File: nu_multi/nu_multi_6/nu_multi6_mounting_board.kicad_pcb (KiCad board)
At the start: 2 copper layers, 70 x 18.2 mm, 14 parts, among them J1 CONN_01X02, J10 CONN_01X03, J11 CONN_01X02, J12 CONN_01X03, J13 CONN_01X14, J2 CONN_01X03, J3 CONN_01X02, J4 CONN_01X03, J5 CONN_01X02, J6 CONN_01X03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

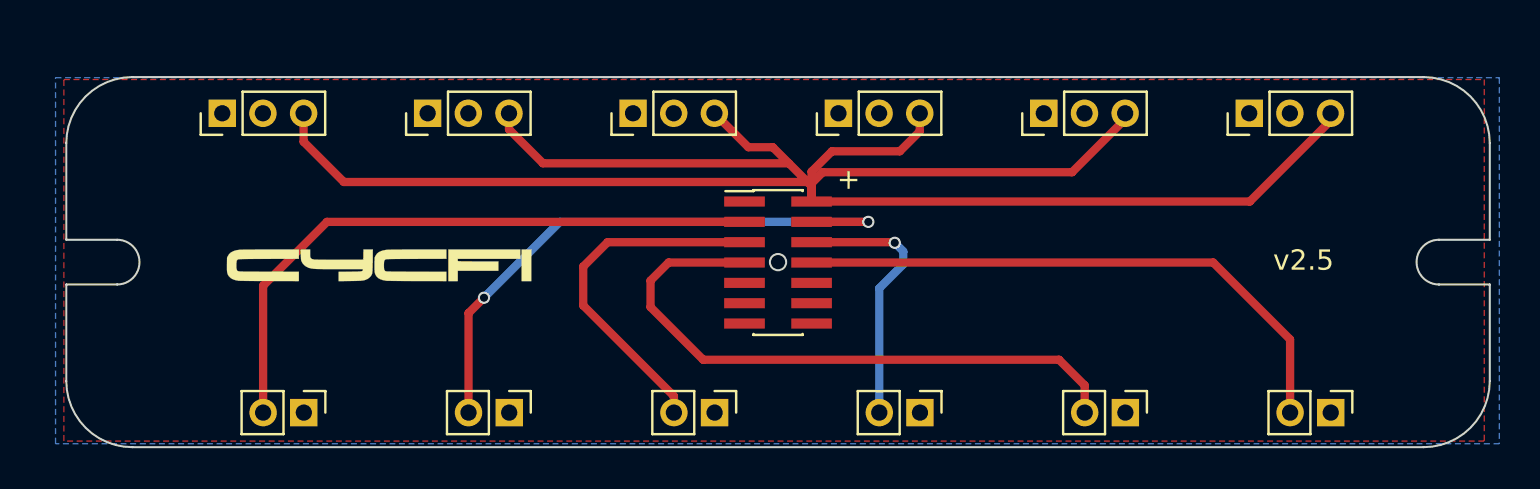
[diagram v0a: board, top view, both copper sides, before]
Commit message: perfect alignment; fixed sloppy positioning
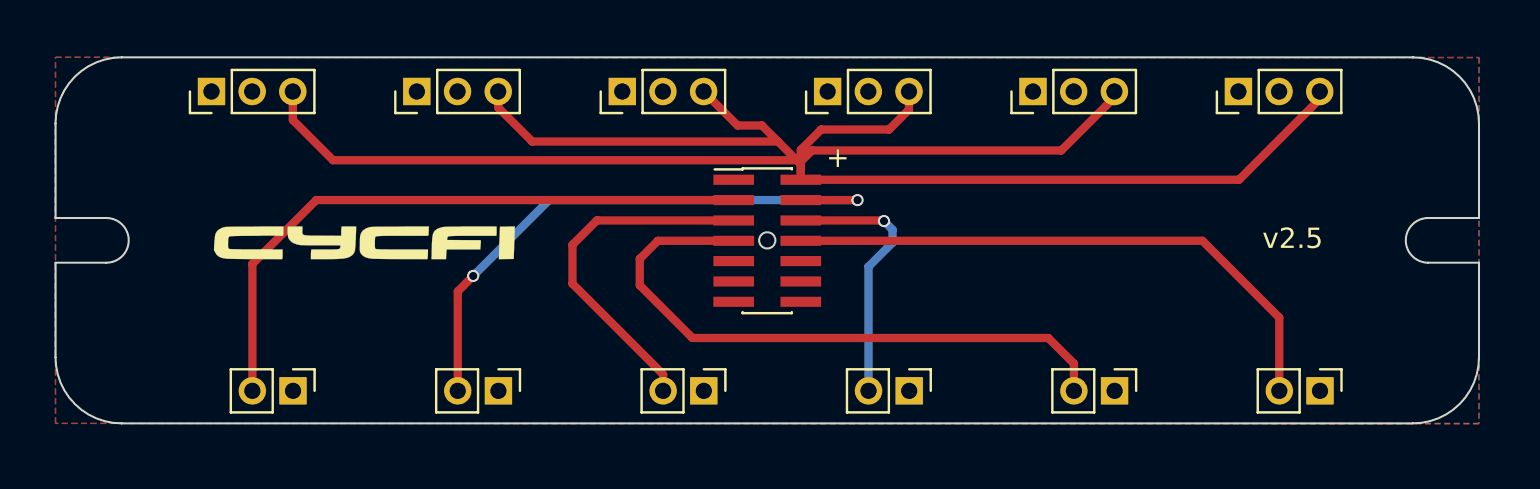
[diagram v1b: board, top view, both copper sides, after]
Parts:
- removed the G*** at (120.9, 94.2)
- added G***: LOGO, cycfi_library:cycfi-logo-15mm, F.Cu at (120.1, 93.2)
- moved J13 1.19 mm to (140.0, 93.0)
- moved J1 1.19 mm to (157.1, 100.4)
- moved J10 1.19 mm to (112.7, 85.7)
- moved J11 1.19 mm to (167.2, 100.4)
- moved J12 1.19 mm to (163.2, 85.7)
- moved J2 1.19 mm to (153.1, 85.7)
- moved J3 1.19 mm to (147.0, 100.4)
- moved J4 1.19 mm to (143.0, 85.7)
- moved J5 1.19 mm to (136.9, 100.4)
- moved J6 1.19 mm to (132.9, 85.7)
- moved J7 1.19 mm to (126.8, 100.4)
- moved J8 1.19 mm to (122.8, 85.7)
- moved J9 1.19 mm to (116.7, 100.4)
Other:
- board size 70 x 18.2 mm -> 70 x 18 mm

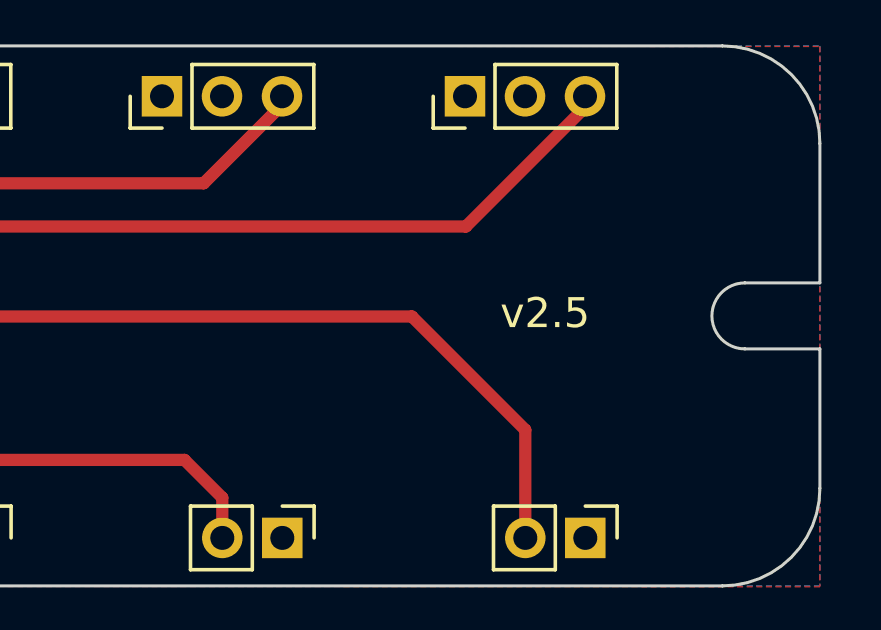
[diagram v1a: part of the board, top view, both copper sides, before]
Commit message: Updates; added nu multi-8 mounting board
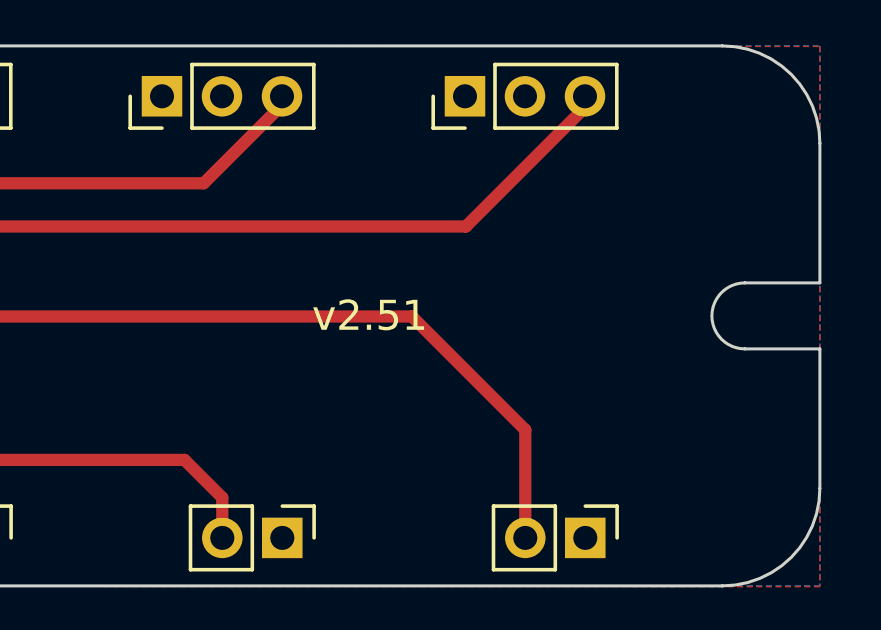
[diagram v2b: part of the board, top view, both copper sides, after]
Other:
- board text added: "v2.51"
- board text removed: "v2.5"

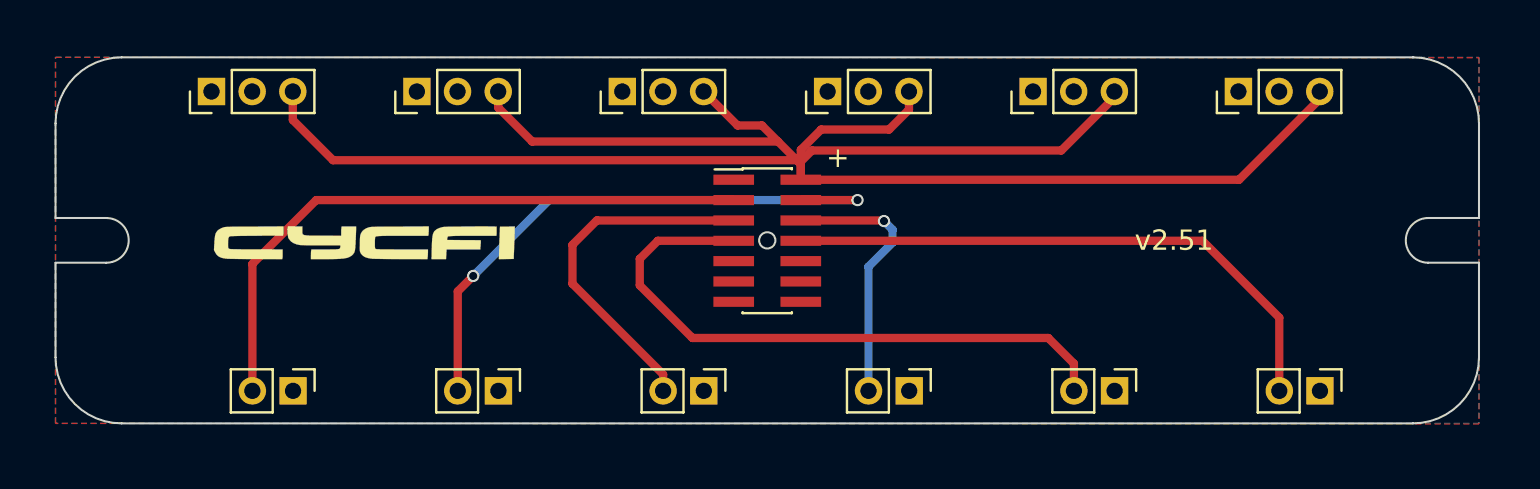
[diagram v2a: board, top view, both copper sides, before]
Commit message: Upgrade to KiCad 6
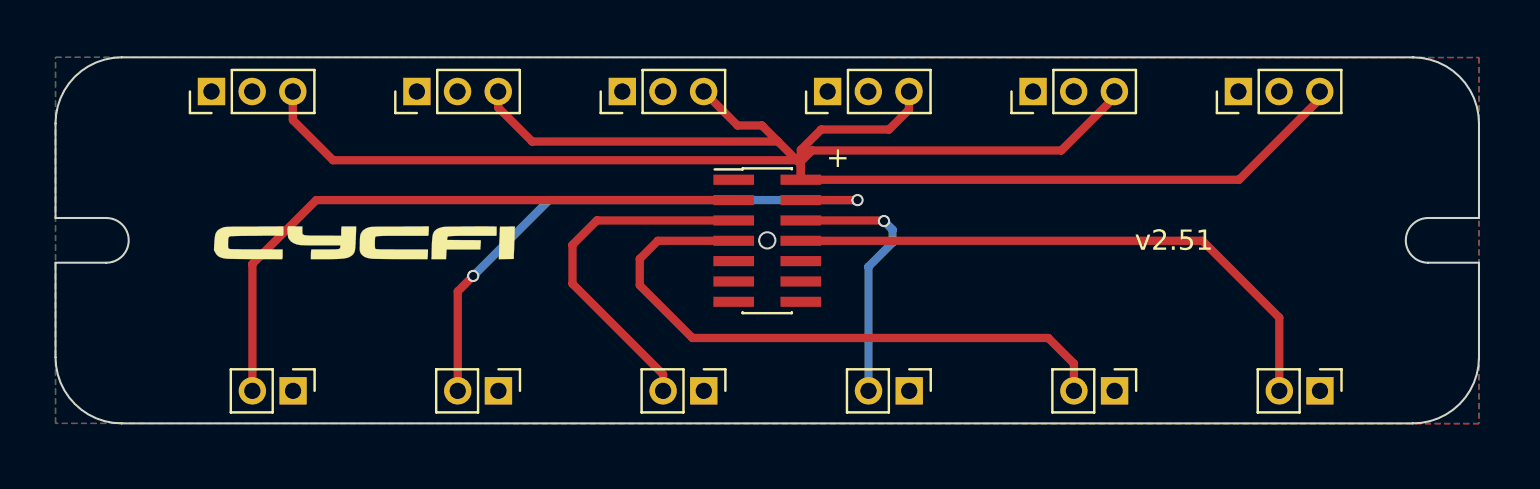
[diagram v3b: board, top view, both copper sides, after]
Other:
- net class Default removed

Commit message: Upgraded schematics and PCB layout using Nu Capsule footprint
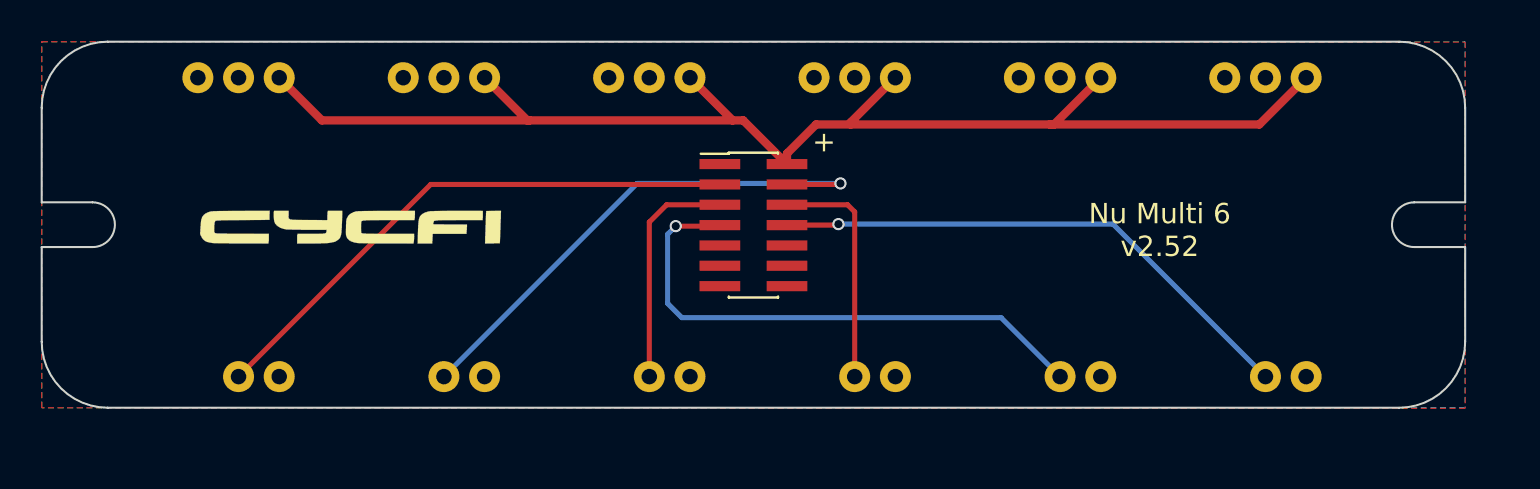
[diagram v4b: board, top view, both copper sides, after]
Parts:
- removed J1, J11, J3, J5, J7, J9: CONN_01X02, Pin_Headers:Pin_Header_Straight_1x02_Pitch2.00mm
- removed J10, J12, J2, J4, J6, J8: CONN_01X03, Pin_Headers:Pin_Header_Straight_1x03_Pitch2.00mm
- added U1: nu_capsule, cycfi_library:nu_capsule, F.Cu at (112.0, 85.0)
- added U2: nu_capsule, cycfi_library:nu_capsule, F.Cu at (122.1, 85.0)
- added U3: nu_capsule, cycfi_library:nu_capsule, F.Cu at (132.2, 85.0)
- added U4: nu_capsule, cycfi_library:nu_capsule, F.Cu at (142.3, 85.0)
- added U5: nu_capsule, cycfi_library:nu_capsule, F.Cu at (152.4, 85.0)
- added U6: nu_capsule, cycfi_library:nu_capsule, F.Cu at (162.5, 85.0)
- moved G*** 1.03 mm to (119.4, 92.4)
- moved J13 1.03 mm to (139.3, 92.2)
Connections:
- J13 pad 10: Net-(J13-Pad10) -> unconnected-(J13-Pad10)
- J13 pad 3: Net-(J13-Pad3) -> CH1
- J13 pad 4: Net-(J13-Pad4) -> CH2
- J13 pad 5: Net-(J13-Pad5) -> CH3
- J13 pad 6: Net-(J13-Pad6) -> CH4
- J13 pad 7: Net-(J1-Pad2) -> CH5
- J13 pad 8: Net-(J11-Pad2) -> CH6
- J13 pad 9: Net-(J13-Pad9) -> unconnected-(J13-Pad9)
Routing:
- net V+: track 102.5 -> 67.0 mm
- net Net-(J13-Pad3): track 31.2 -> 0.00 mm
- net Net-(J1-Pad2): track 30.6 -> 0.00 mm
- net Net-(J13-Pad4): track 29.2 -> 0.00 mm, vias 2 -> 0
- net Net-(J11-Pad2): track 28.7 -> 0.00 mm
- net CH1: track 0.00 -> 27.6 mm
- net CH5: track 0.00 -> 26.9 mm, vias 0 -> 1
- net CH6: track 0.00 -> 26.7 mm, vias 0 -> 1
- net CH2: track 0.00 -> 26.1 mm, vias 0 -> 1
- net Net-(J13-Pad5): track 17.5 -> 0.00 mm
- net Net-(J13-Pad6): track 13.1 -> 0.00 mm, vias 1 -> 0
- net CH4: track 0.00 -> 11.6 mm
- net CH3: track 0.00 -> 11.4 mm
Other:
- outline, holes or cut-outs redrawn
- board text added: "Nu Multi 6 v2.52"
- board text removed: "v2.51"

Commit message: Updated edge-cuts from dxf file
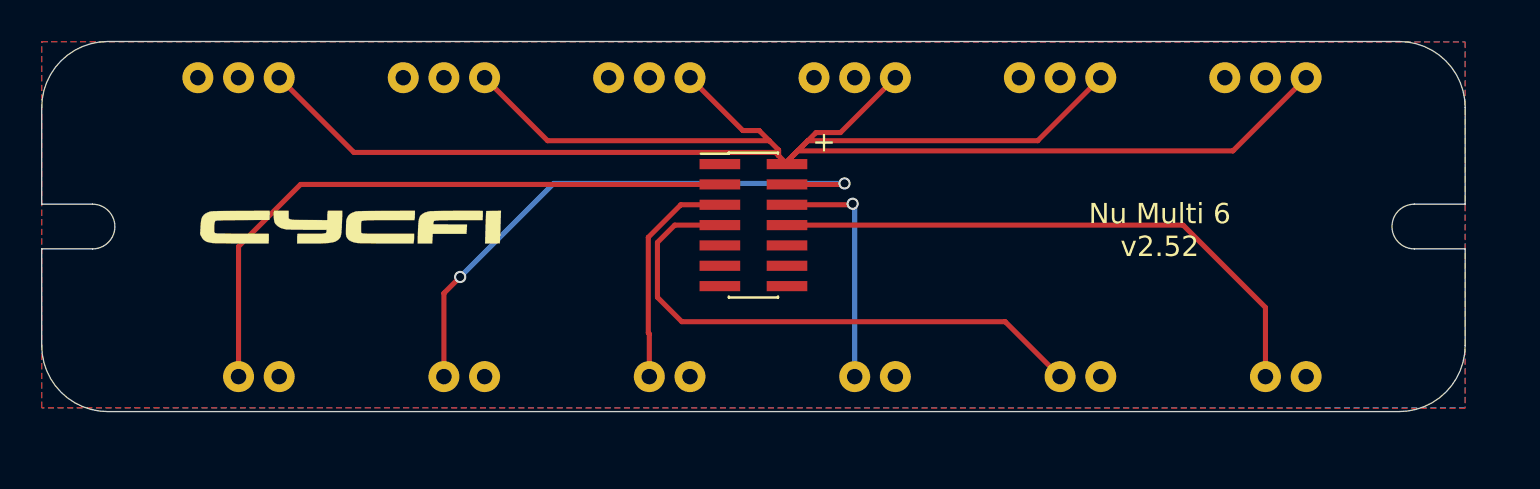
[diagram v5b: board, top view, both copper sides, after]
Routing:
- net V+: track 67.0 -> 99.3 mm
- net CH1: track 27.6 -> 31.3 mm
- net CH2: track 26.1 -> 28.9 mm, vias 1 -> 2
- net CH6: track 26.7 -> 28.6 mm, vias 1 -> 0
- net CH5: track 26.9 -> 27.5 mm, vias 1 -> 0
- net CH4: track 11.6 -> 11.8 mm, vias 0 -> 1
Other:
- board size 70 x 18 mm -> 70 x 18.2 mm
